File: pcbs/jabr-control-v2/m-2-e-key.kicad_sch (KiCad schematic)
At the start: 8 parts, among them J4001 MDT320E0X001, Y401 ASEK-32.768KHZ-LRT

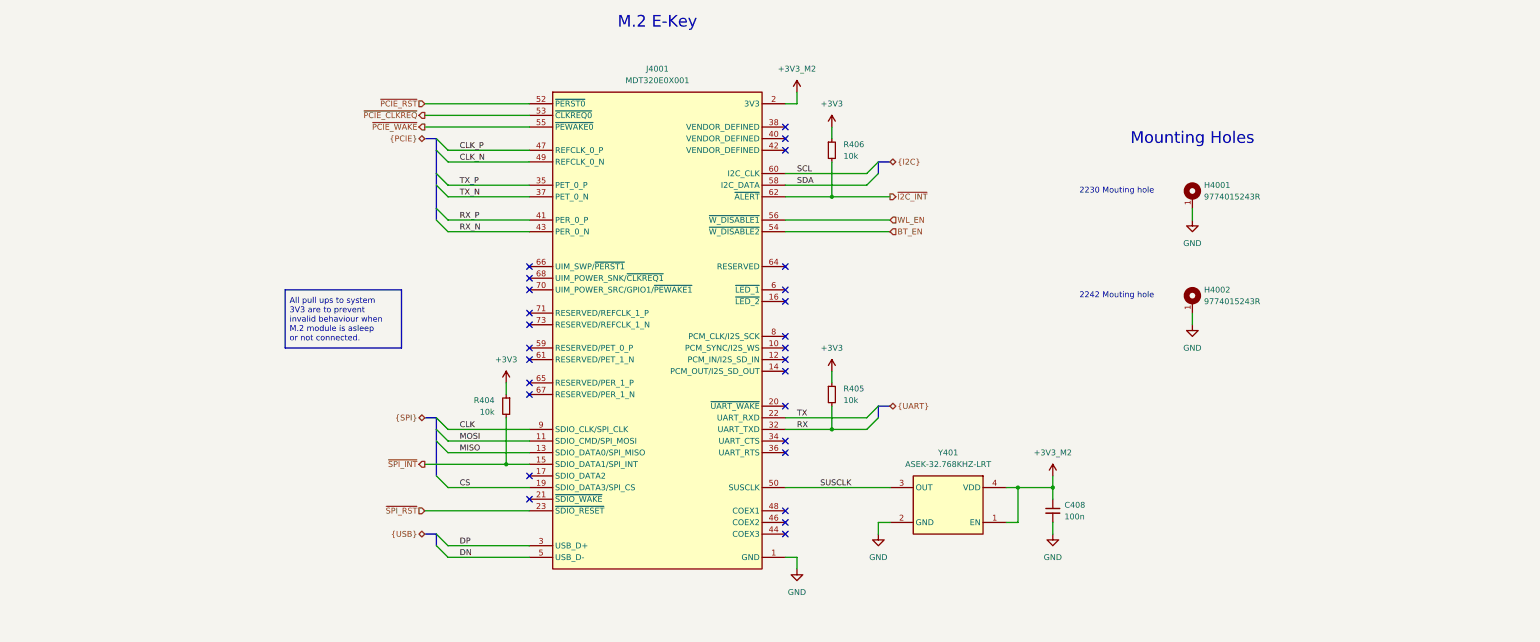
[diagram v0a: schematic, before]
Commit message: PCI11010C Schematic sheet mostly done
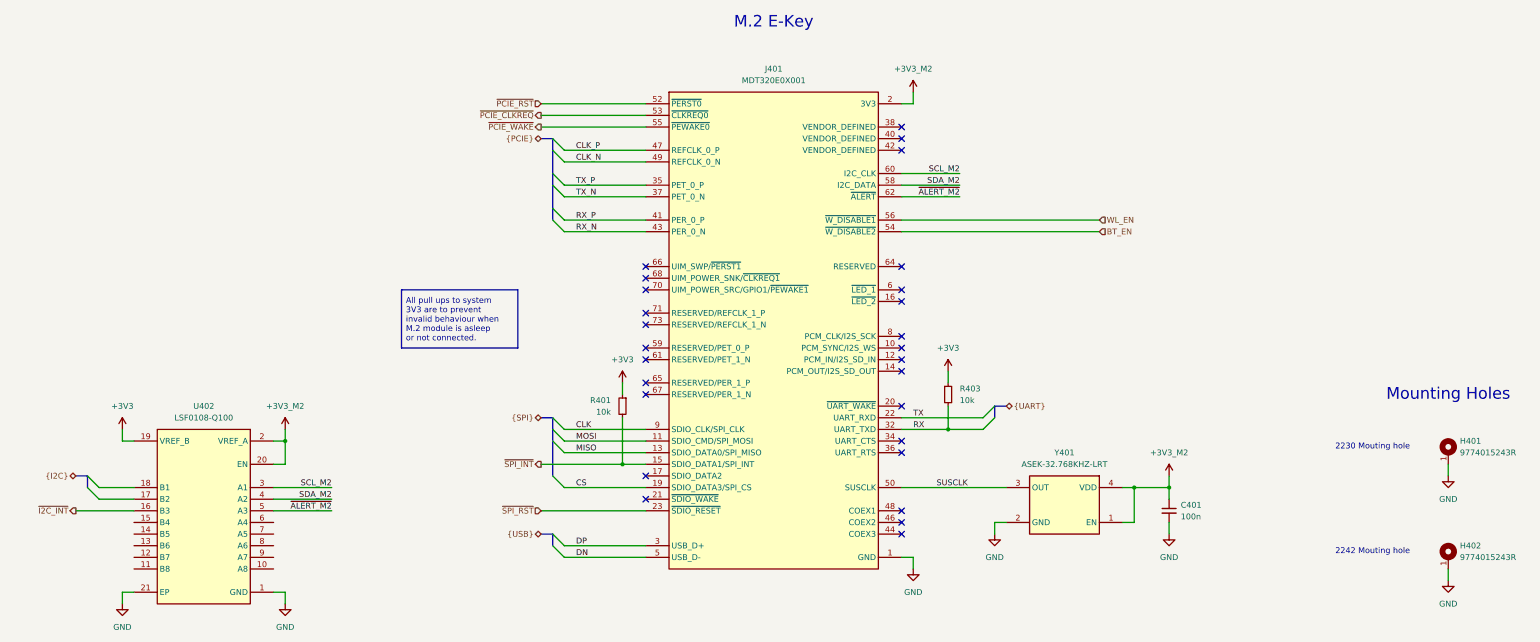
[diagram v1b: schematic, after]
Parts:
- removed R406: 10k, project_footprints:R_0402, symbol DEV:R_SMALL
- added U402: LSF0108-Q100, project_footprints:LSF0108BQ-Q100X, symbol COMM-BUF:LSF0108-Q100
- renumbered C408 to C401, H4001 to H401, H4002 to H402, J4001 to J401, R404 to R401, R405 to R403
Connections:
- net +3V3: now also U402.19 (VREF_B)
- net +3V3_M2: now also U402.2 (VREF_A), U402.20 (EN)
- net GND: now also U402.1 (GND), U402.21 (EP)
- net ~{I2C_INT}: now also U402.16 (B3); no longer J401.62 (~{ALERT})
- net SCL renamed SCL_M2
- net SCL_M2: now also U402.3 (A1)
- net SDA renamed SDA_M2
- net SDA_M2: now also U402.4 (A2)
- new net ~{ALERT_M2}: J401.62 (~{ALERT}), U402.5 (A3)
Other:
- moved on the sheet: C401, H401, H402, J401, R401, R403, Y401

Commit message: Moved M.2 buffers to new sheet
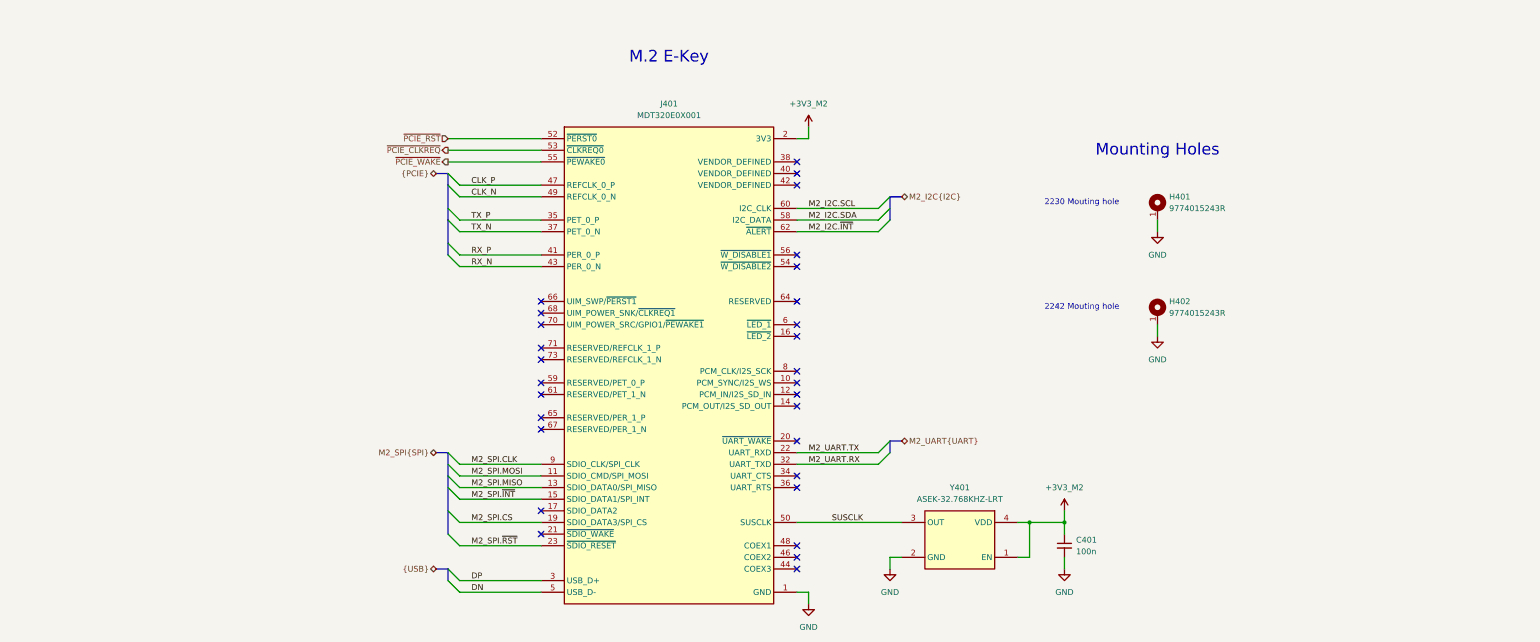
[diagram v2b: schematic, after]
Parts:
- removed R401, R403: 10k, project_footprints:R_0402, symbol DEV:R_SMALL
- removed U402: LSF0108-Q100, project_footprints:LSF0108BQ-Q100X, symbol COMM-BUF:LSF0108-Q100
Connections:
- net BT_EN: no longer names the net of J401.54 (~{W_DISABLE2})
- net CLK renamed M2_SPI.CLK
- net CS renamed M2_SPI.CS
- net MISO renamed M2_SPI.MISO
- net MOSI renamed M2_SPI.MOSI
- net RX renamed M2_UART.RX
- net SCL_M2 renamed M2_I2C.SCL
- net SDA_M2 renamed M2_I2C.SDA
- net TX renamed M2_UART.TX
- net WL_EN: no longer names the net of J401.56 (~{W_DISABLE1})
- net ~{ALERT_M2} renamed M2_I2C.~{INT}
- net ~{SPI_INT} renamed M2_SPI.~{INT}
- net ~{SPI_RST} renamed M2_SPI.~{RST}
- no-connect marks 27 -> 29
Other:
- moved on the sheet: C401, H401, H402, J401, Y401

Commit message: PCI11010 IO done
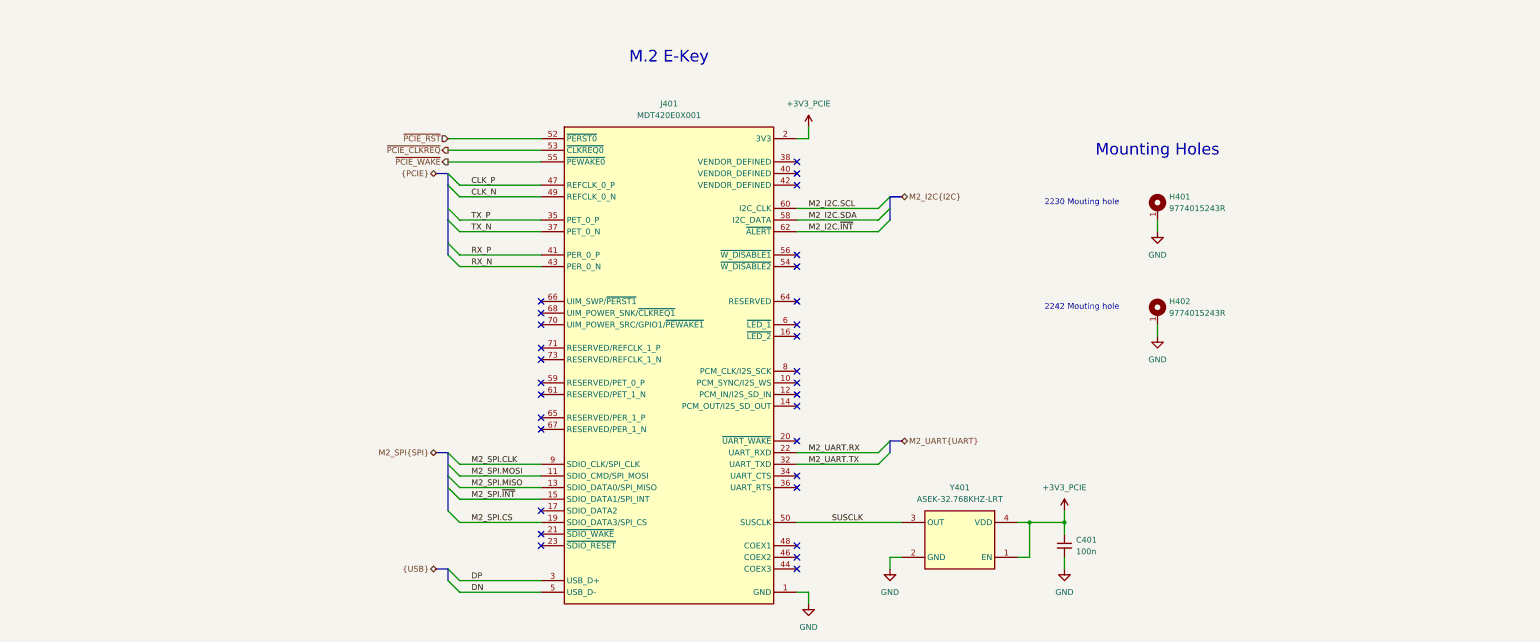
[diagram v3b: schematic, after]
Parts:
- J401: value MDT320E0X001 -> MDT420E0X001
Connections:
- net M2_UART.RX: now also J401.22 (UART_RXD); no longer J401.32 (UART_TXD)
- net M2_UART.TX: now also J401.32 (UART_TXD); no longer J401.22 (UART_RXD)
- net +3V3_M2 renamed +3V3_PCIE
- net M2_SPI.~{RST}: no longer names the net of J401.23 (~{SDIO_RESET})
- no-connect marks 29 -> 30
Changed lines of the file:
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@@
+	)
+	(no_connect
+		(at 101.6 142.24)
 	)
 	(no_connect
@@
 	)
 	(bus_entry
-		(at 81.28 139.7)
-		(size 2.54 2.54)
-		(stroke
-			(width 0)
-			(type default)
-		)
-	)
-	(bus_entry
 		(at 81.28 147.32)
 		(size 2.54 2.54)
@@
 	(wire
 		(pts
-			(xy 83.82 142.24) (xy 101.6 142.24)
-		)
-		(stroke
-			(width 0)
-			(type default)
-		)
-	)
-	(wire
-		(pts
 			(xy 83.82 129.54) (xy 101.6 129.54)
 		)
@@
 		)
 	)
+	(bus
+		(pts
+			(xy 81.28 121.92) (xy 81.28 134.62)
+		)
+		(stroke
+			(width 0)
+			(type default)
+		)
+	)
 	(wire
 		(pts
@@
 		(pts
 			(xy 83.82 152.4) (xy 101.6 152.4)
-		)
-		(stroke
-			(width 0)
-			(type default)
-		)
-	)
-	(bus
-		(pts
-			(xy 81.28 121.92) (xy 81.28 139.7)
 		)
 		(stroke
@@
 	)
 	(label "M2_UART.TX"
-		(at 160.02 121.92 0)
+		(at 160.02 124.46 0)
 		(effects
 			(font
@@
 		)
 	)
-	(label "M2_SPI.~{RST}"
-		(at 86.36 142.24 0)
-		(effects
-			(font
-				(size 1.27 1.27)
-			)
-			(justify left bottom)
-		)
-	)
 	(label "SUSCLK"
 		(at 165.1 137.16 0)
@@
 	)
 	(label "M2_UART.RX"
-		(at 160.02 124.46 0)
+		(at 160.02 121.92 0)
 		(effects
 			(font
@@
 			)
 		)
-		(property "Value" "MDT320E0X001"
+		(property "Value" "MDT420E0X001"
 			(at 129.54 48.26 0)
 			(show_name no)
@@
 		)
 		(property "Datasheet" "https://cdn.amphenol-cs.com/media/wysiwyg/files/documentation/datasheet/ssio/ssio_pcie_m2.pdf"
-			(at 224.79 240.64 0)
-			(hide yes)
-			(show_name no)
-			(do_not_autoplace no)
-			(effects
-				(font
-					(size 1.27 1.27)
-				)
-				(justify left top)
+			(at 129.54 162.56 0)
+			(hide yes)
+			(show_name no)
+			(do_not_autoplace no)
+			(effects
+				(font
+					(size 1.27 1.27)
+				)
 			)
 		)
@@
 	)
 	(symbol
-		(lib_id "PWR-SYM:+3V3_M2")
+		(lib_id "PWR-SYM:+3V3_PCIE")
 		(at 160.02 50.8 0)
 		(unit 1)
@@
 		(dnp no)
 		(fields_autoplaced yes)
-		(property "Reference" "#PWR0401"
+		(property "Reference" "#PWR0408"
 			(at 160.02 54.61 0)
 			(hide yes)
@@
 			)
 		)
-		(property "Value" "+3V3_M2"
+		(property "Value" "+3V3_PCIE"
 			(at 160.02 45.72 0)
 			(show_name no)
@@
 			)
 		)
-		(property "Description" "Power symbol creates a global label with name \"+3V3_M2\""
+		(property "Description" "Power symbol creates a global label with name \"+3V3_PCIE\""
 			(at 160.02 50.8 0)
+			(hide yes)
+			(show_name no)
+			(do_not_autoplace no)
+			(effects
+				(font
+					(size 1.27 1.27)
+				)
+			)
+		)
+		(pin "1"
+		)
+		(instances
+			(project "jabr-control-v2"
+				(path "/f91ec272-d09a-4038-bbbb-962739a92c51/1d5b5326-5e18-44b7-8507-f118df052f59"
+					(reference "#PWR0408")
+					(unit 1)
+				)
+			)
+		)
+	)
+	(symbol
+		(lib_id "PWR-SYM:+3V3_PCIE")
+		(at 215.9 134.62 0)
+		(unit 1)
+		(body_style 1)
+		(exclude_from_sim no)
+		(in_bom yes)
+		(on_board yes)
+		(in_pos_files yes)
+		(dnp no)
+		(fields_autoplaced yes)
+		(property "Reference" "#PWR0401"
+			(at 215.9 138.43 0)
+			(hide yes)
+			(show_name no)
+			(do_not_autoplace no)
+			(effects
+				(font
+					(size 1.27 1.27)
+				)
+			)
+		)
+		(property "Value" "+3V3_PCIE"
+			(at 215.9 129.54 0)
+			(show_name no)
+			(do_not_autoplace no)
+			(effects
+				(font
+					(size 1.27 1.27)
+				)
+			)
+		)
+		(property "Footprint" ""
+			(at 215.9 134.62 0)
+			(hide yes)
+			(show_name no)
+			(do_not_autoplace no)
+			(effects
+				(font
+					(size 1.27 1.27)
+				)
+			)
+		)
+		(property "Datasheet" ""
+			(at 215.9 134.62 0)
+			(hide yes)
+			(show_name no)
+			(do_not_autoplace no)
+			(effects
+				(font
+					(size 1.27 1.27)
+				)
+			)
+		)
+		(property "Description" "Power symbol creates a global label with name \"+3V3_PCIE\""
+			(at 215.9 134.62 0)
 			(hide yes)
 			(show_name no)
@@
 					(unit 1)
 				)
-			)
-		)
-	)
-	(symbol
-		(lib_id "PWR-SYM:+3V3_M2")
-		(at 215.9 134.62 0)
-		(unit 1)
-		(body_style 1)
-		(exclude_from_sim no)
-		(in_bom yes)
-		(on_board yes)
-		(in_pos_files yes)
-		(dnp no)
-		(fields_autoplaced yes)
-		(property "Reference" "#PWR0404"
-			(at 215.9 138.43 0)
-			(hide yes)
-			(show_name no)
-			(do_not_autoplace no)
-			(effects
-				(font
-					(size 1.27 1.27)
-				)
-			)
-		)
-		(property "Value" "+3V3_M2"
-			(at 215.9 129.54 0)
-			(show_name no)
-			(do_not_autoplace no)
-			(effects
-				(font
-					(size 1.27 1.27)
-				)
-			)
-		)
-		(property "Footprint" ""
-			(at 215.9 134.62 0)
-			(hide yes)
-			(show_name no)
-			(do_not_autoplace no)
-			(effects
-				(font
-					(size 1.27 1.27)
-				)
-			)
-		)
-		(property "Datasheet" ""
-			(at 215.9 134.62 0)
-			(hide yes)
-			(show_name no)
-			(do_not_autoplace no)
-			(effects
-				(font
-					(size 1.27 1.27)
-				)
-			)
-		)
-		(property "Description" "Power symbol creates a global label with name \"+3V3_M2\""
-			(at 215.9 134.62 0)
-			(hide yes)
-			(show_name no)
-			(do_not_autoplace no)
-			(effects
-				(font
-					(size 1.27 1.27)
-				)
-			)
-		)
-		(pin "1"
-		)
-		(instances
-			(project "jabr-control-v2"
-				(path "/f91ec272-d09a-4038-bbbb-962739a92c51/1d5b5326-5e18-44b7-8507-f118df052f59"
-					(reference "#PWR0404")
-					(unit 1)
-				)

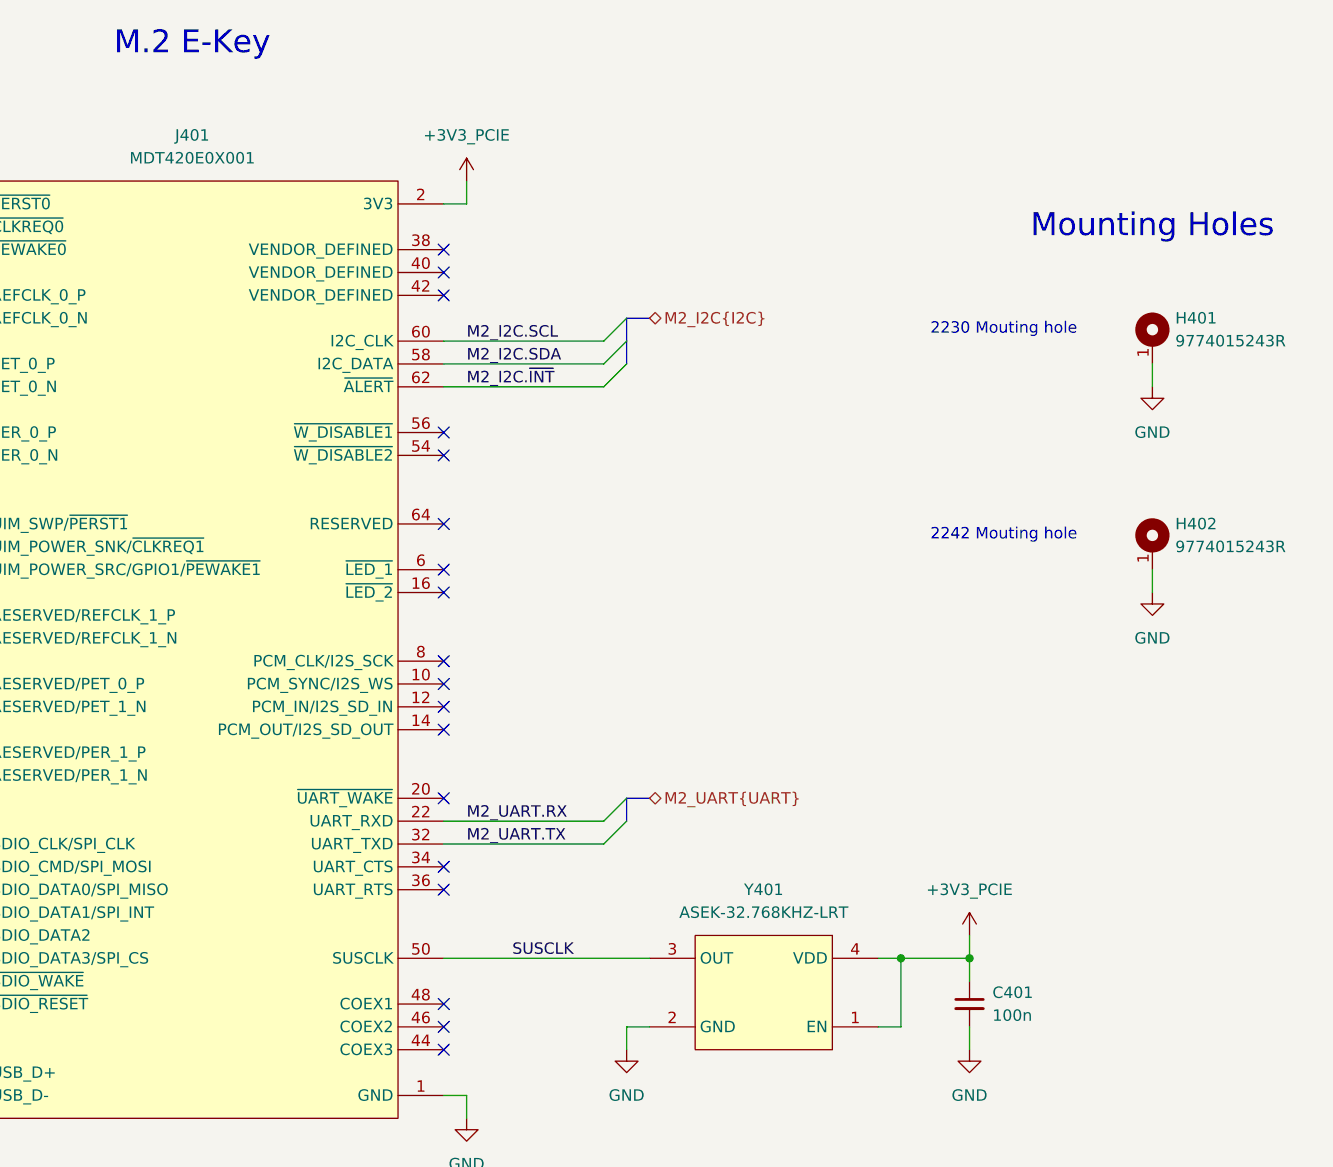
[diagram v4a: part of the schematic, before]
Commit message: Schematic done
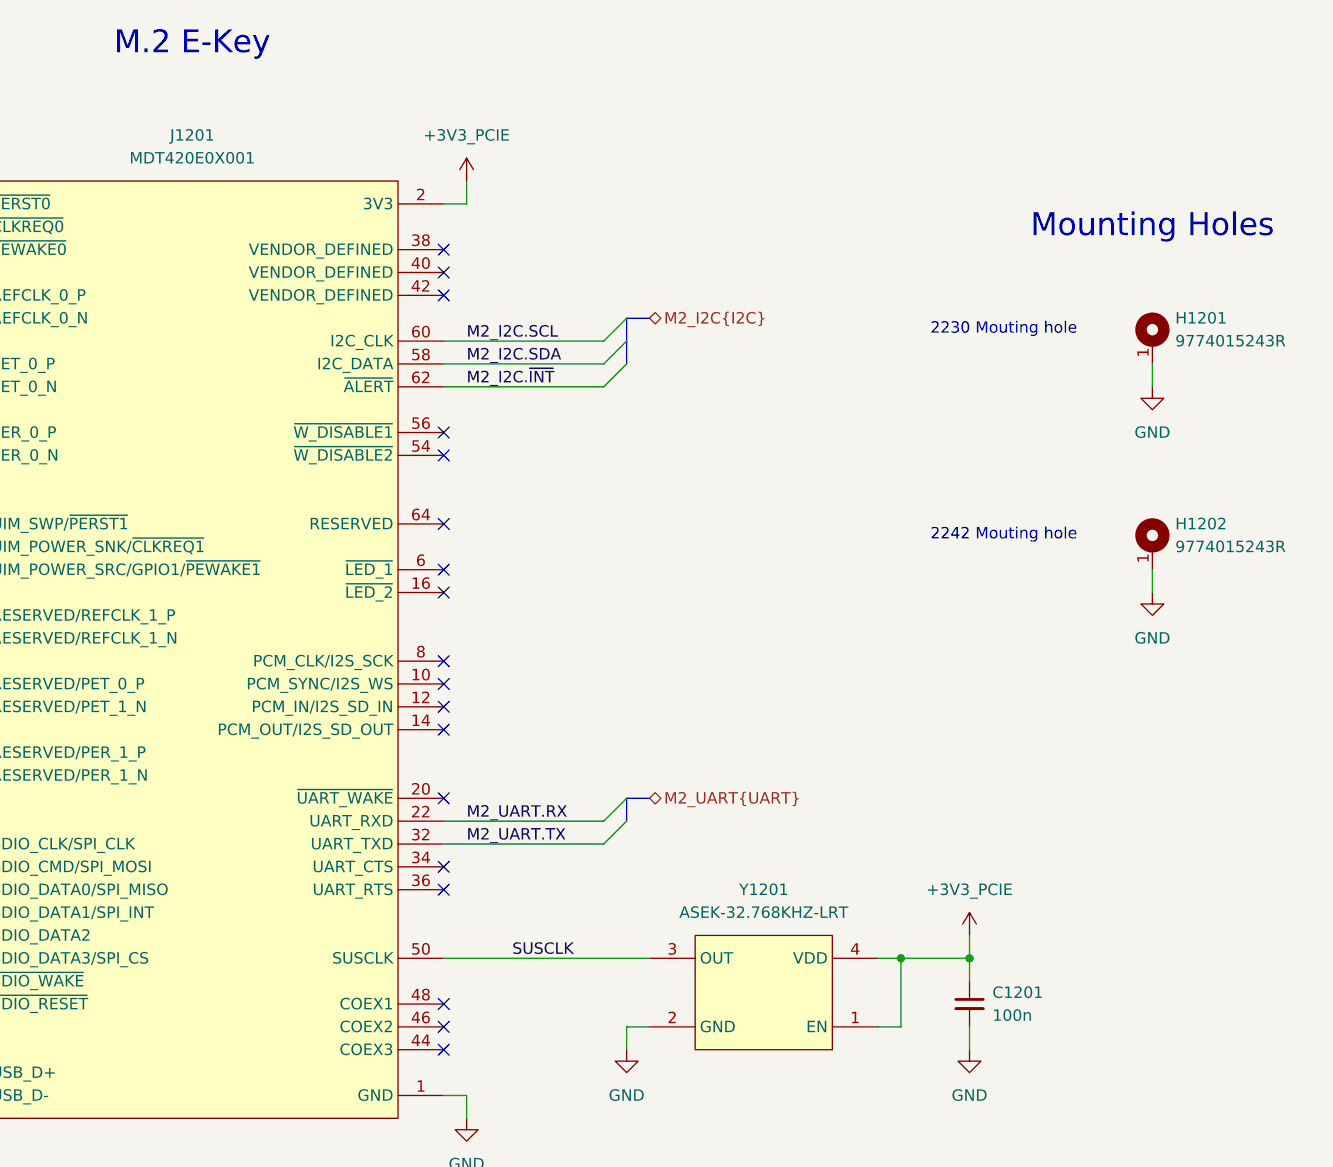
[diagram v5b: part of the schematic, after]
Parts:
- C1201: renamed from C401; footprint (none) -> project_footprints:C_0402
- renumbered H401 to H1201, H402 to H1202, J401 to J1201, Y401 to Y1201
